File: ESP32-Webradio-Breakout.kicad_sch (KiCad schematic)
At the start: 46 parts, among them J1 AudioJack3, J2 Conn_01x02, P1 USB_C_Plug, Q1 BC817, Q2 BC817, Q3 BC817, SW1 RotaryEncoder_Switch, U1 AMS1117-3.3, U2 ESP32-WROOM-32, U3 CH340C, U4 PCF8574TS, U5 DS18B20

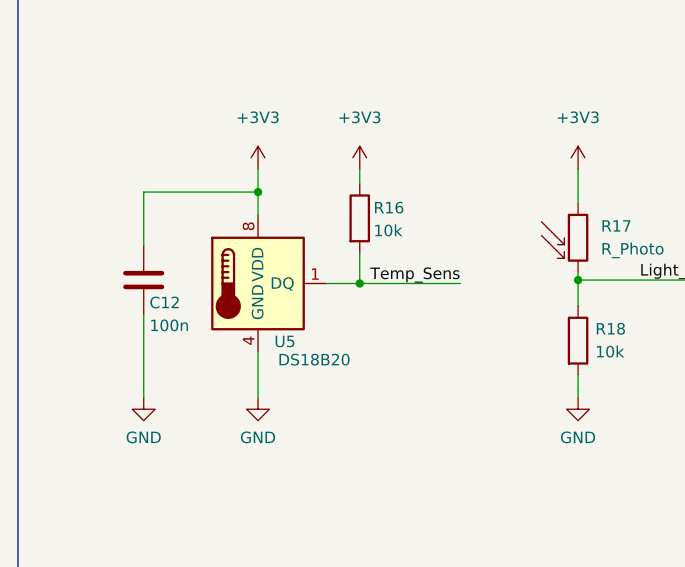
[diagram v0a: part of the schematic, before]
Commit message: Parts placement top side
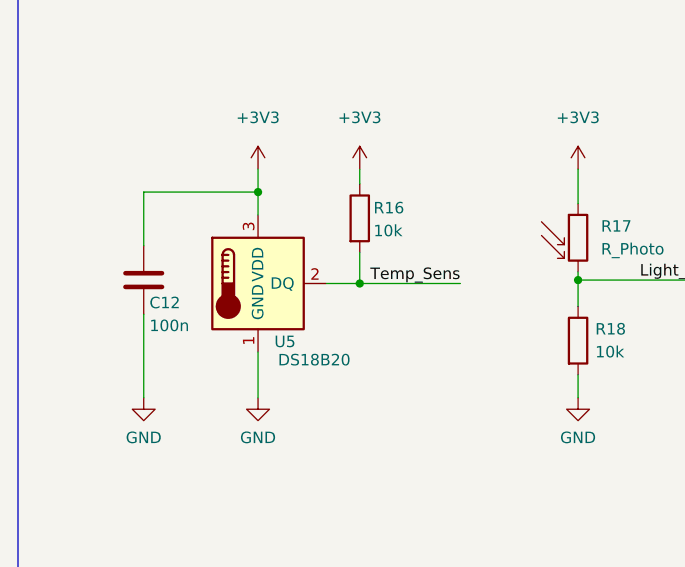
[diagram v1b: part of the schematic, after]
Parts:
- U5: footprint Package_SO:MSOP-8_3x3mm_P0.65mm -> Connector_PinHeader_2.54mm:PinHeader_1x03_P2.54mm_Vertical; symbol Sensor_Temperature:DS18B20U -> Sensor_Temperature:DS18B20
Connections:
- net +3V3: now also U5.3 (VDD); no longer U5.8 (VDD)
- net GND: now also U5.1 (GND); no longer U5.4 (GND)
- net Temp_Sens: now also U5.2 (DQ); no longer U5.1 (DQ)
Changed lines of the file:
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@@
     (pin "1")
   )
-  (symbol (lib_id "Sensor_Temperature:DS18B20U") (at 64.77 200.66 0) (unit 1)
+  (symbol (lib_id "Sensor_Temperature:DS18B20") (at 64.77 200.66 0) (unit 1)
     (in_bom yes) (on_board yes)
     (property "Reference" "U5" (id 0) (at 68.961 207.137 0)
@@
       (effects (font (size 1.27 1.27)) (justify right))
     )
-    (property "Footprint" "Package_SO:MSOP-8_3x3mm_P0.65mm" (id 2) (at 40.64 207.01 0)
+    (property "Footprint" "Connector_PinHeader_2.54mm:PinHeader_1x03_P2.54mm_Vertical" (id 2) (at 39.37 207.01 0)
       (effects (font (size 1.27 1.27)) hide)
     )
@@
     (pin "2")
     (pin "3")
-    (pin "4")
-    (pin "5")
-    (pin "6")
-    (pin "7")
-    (pin "8")
   )
   (symbol (lib_id "power:VCC") (at 240.03 166.37 0) (unit 1)
@@
     )
     (path "/a6b82443-9372-497e-a356-3173065d1b81"
-      (reference "U5") (unit 1) (value "DS18B20") (footprint "Package_SO:MSOP-8_3x3mm_P0.65mm")
-    )
-  )
+      (reference "U5") (unit 1) (value "DS18B20") (footprint "Connector_PinHeader_2.54mm:PinHeader_1x03_P2.54mm_Vertical")
+    )
+  )

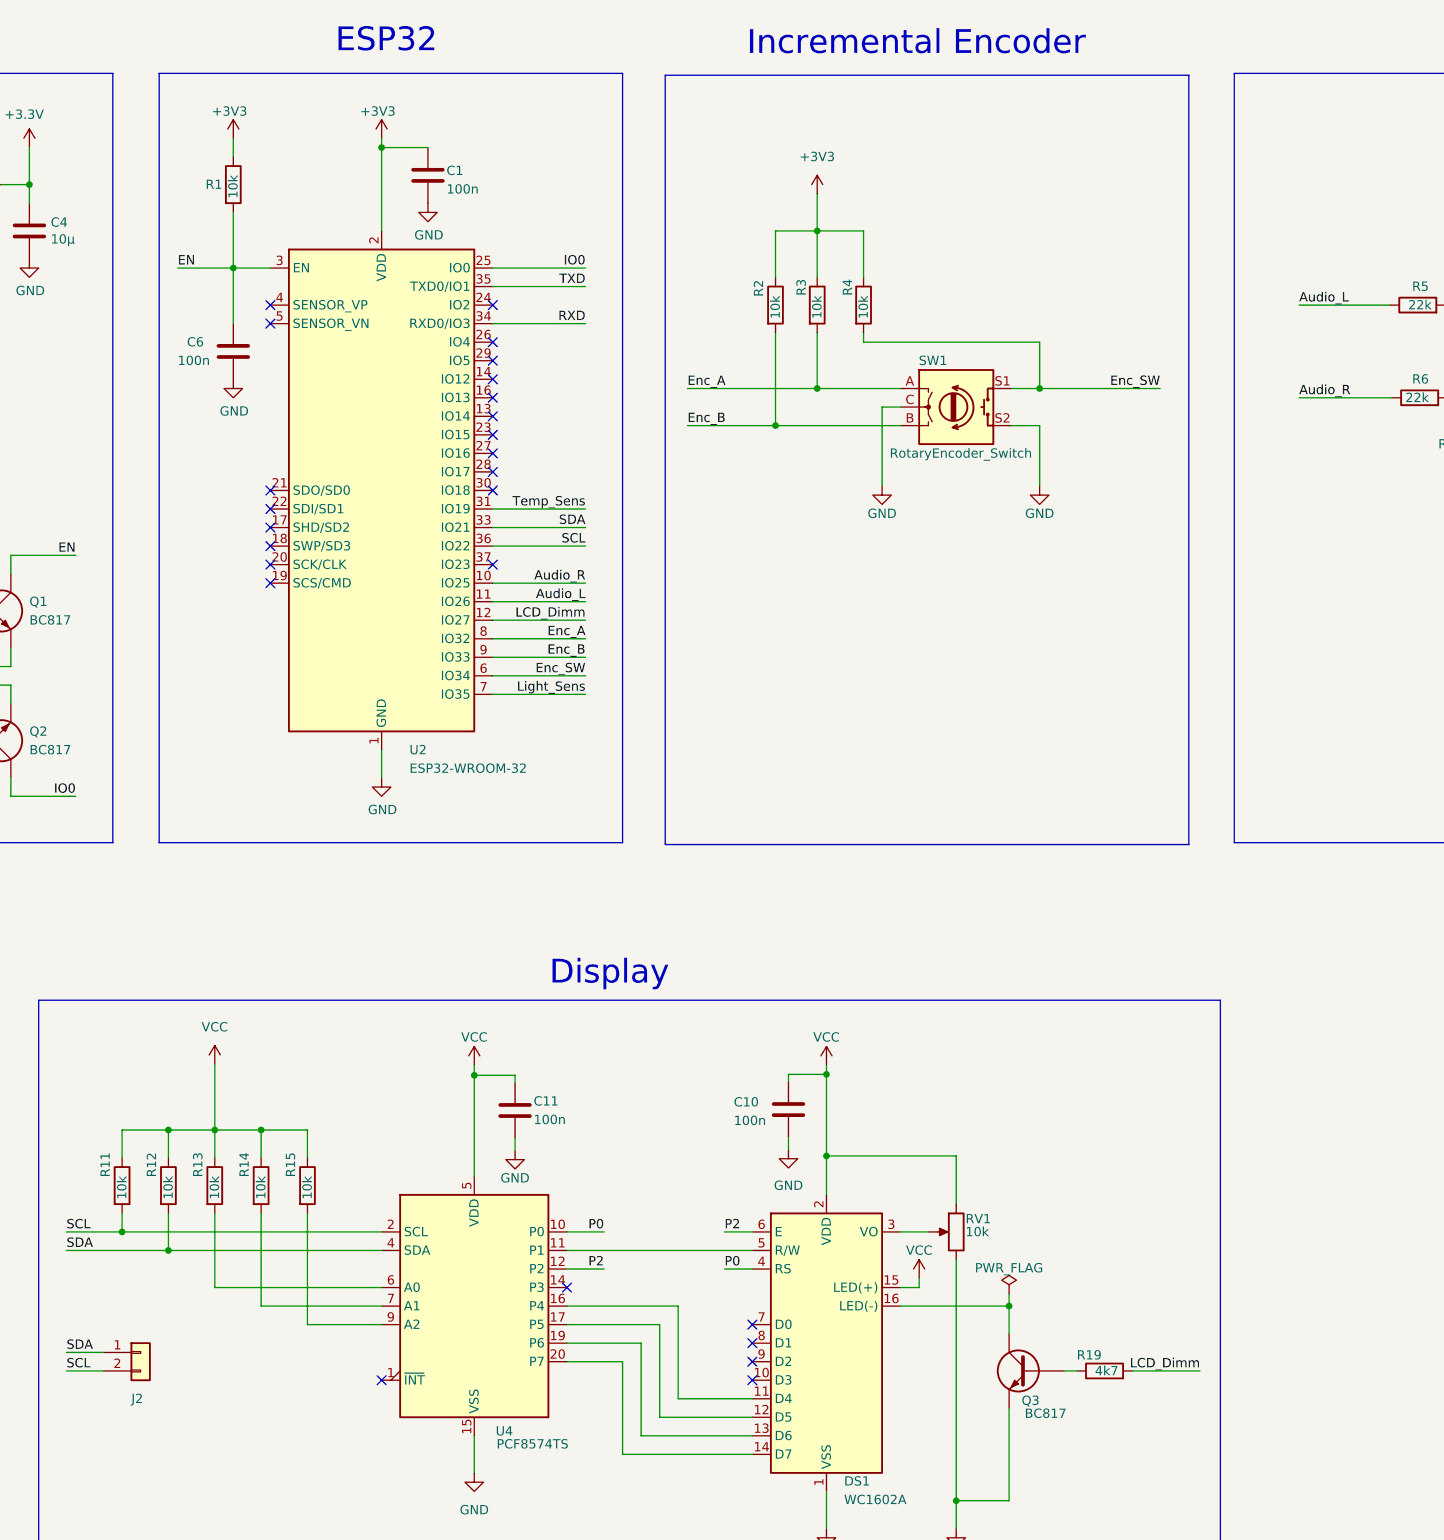
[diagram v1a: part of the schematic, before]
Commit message: Added pin for touch sensor Marked mounting holes as not in schematic
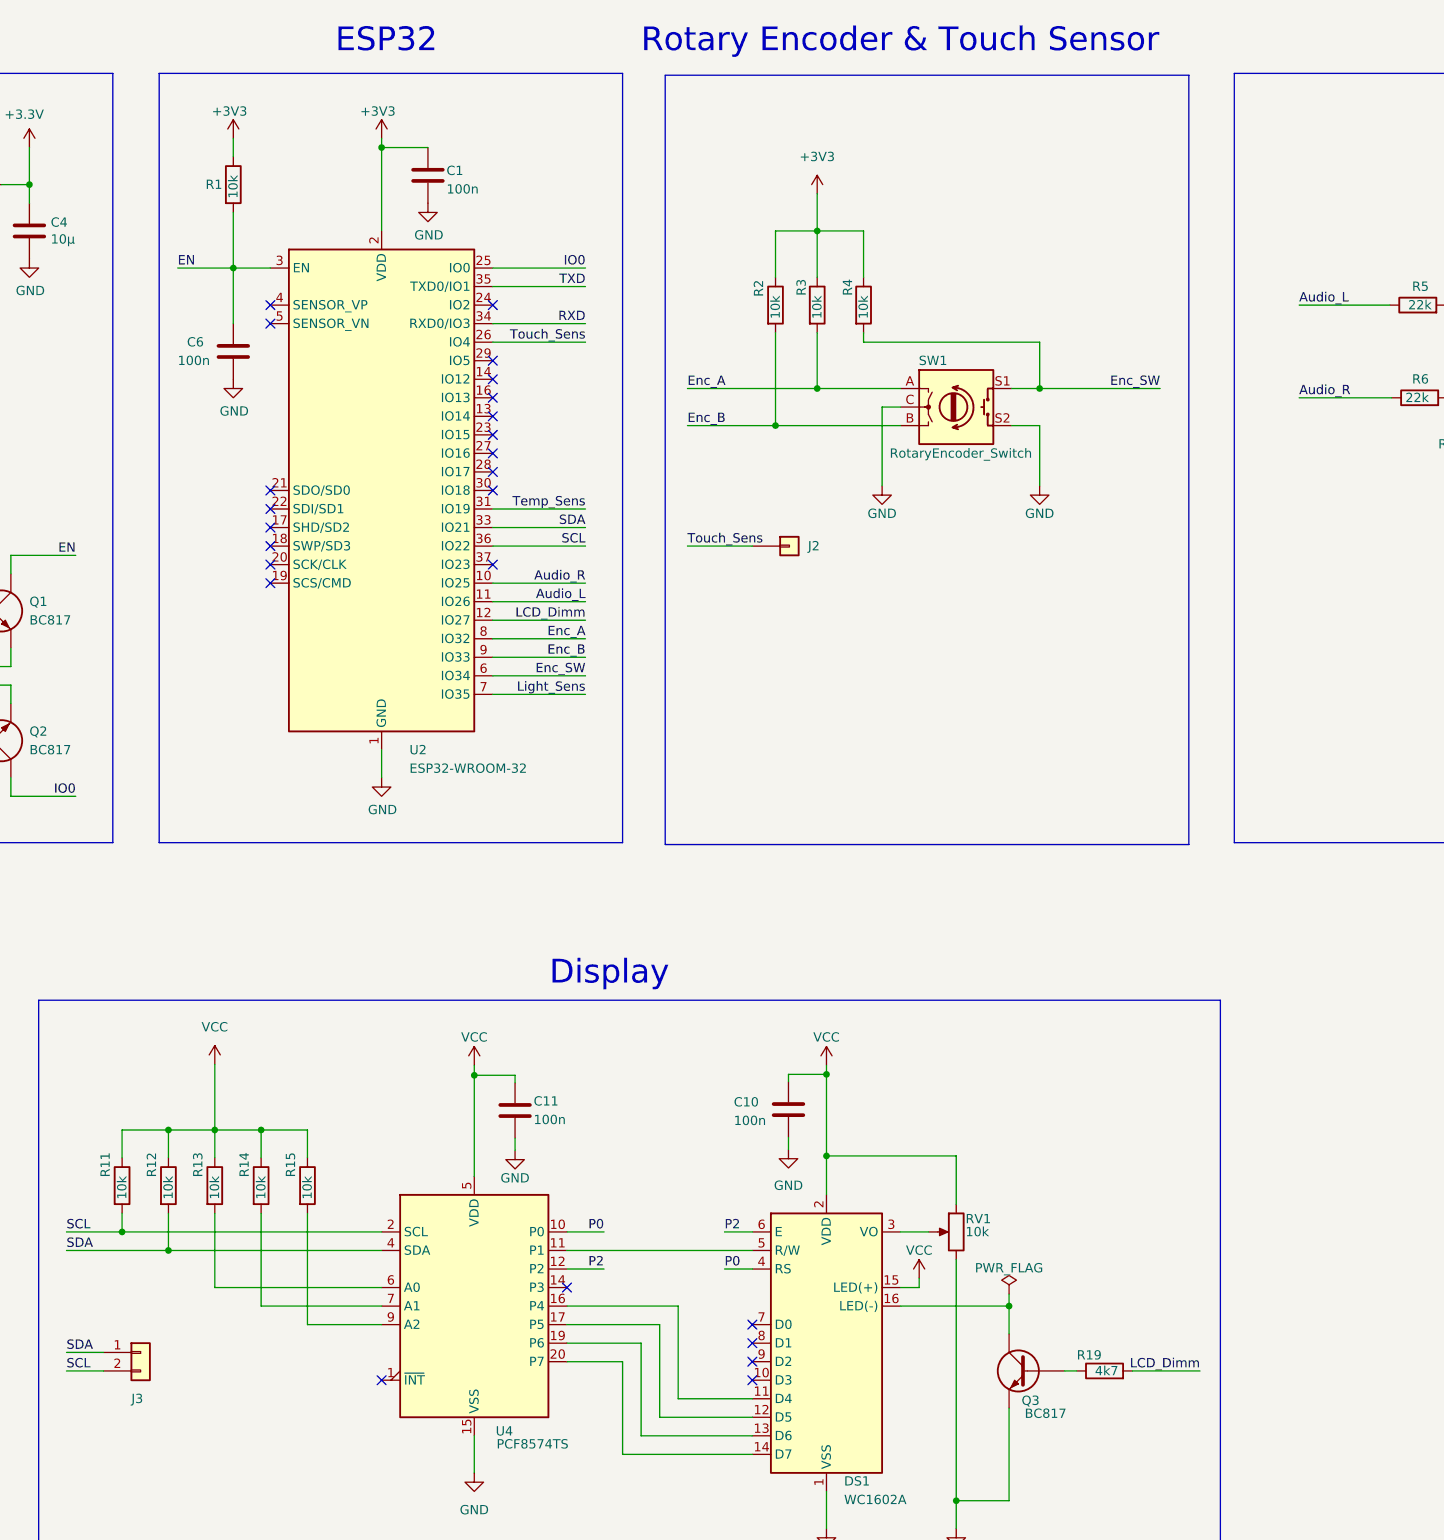
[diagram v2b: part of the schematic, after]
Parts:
- added J2: Conn_01x01, Connector_PinHeader_2.54mm:PinHeader_1x01_P2.54mm_Vertical, symbol Connector_Generic:Conn_01x01
- renumbered J2 to J3
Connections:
- net Touch_Sens: now reaches U2.26 (IO4)
- net Touch_Sens: now also J2.1 (Pin_1)
- no-connect marks 42 -> 41
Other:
- note added: "Rotary Encoder & Touch Sensor"
- note removed: "Incremental Encoder"
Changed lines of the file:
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@@
   (no_connect (at 194.31 77.47))
   (no_connect (at 194.31 74.93))
-  (no_connect (at 194.31 67.31))
   (no_connect (at 163.83 90.17))
   (no_connect (at 194.31 80.01))
@@
     (stroke (width 0) (type default) (color 0 0 0 0))
   )
+  (wire (pts (xy 194.31 67.31) (xy 207.01 67.31))
+    (stroke (width 0) (type default) (color 0 0 0 0))
+  )
   (wire (pts (xy 204.47 201.93) (xy 217.17 201.93))
     (stroke (width 0) (type default) (color 0 0 0 0))
@@
   )
   (wire (pts (xy 88.9 85.09) (xy 102.87 85.09))
+    (stroke (width 0) (type default) (color 0 0 0 0))
+  )
+  (wire (pts (xy 220.98 95.25) (xy 229.87 95.25))
     (stroke (width 0) (type default) (color 0 0 0 0))
   )
@@
     (effects (font (size 3.2512 3.2512)) (justify left bottom))
   )
-  (text "Incremental Encoder" (at 229.108 28.321 0)
+  (text "Rotary Encoder & Touch Sensor" (at 214.63 27.94 0)
     (effects (font (size 3.2512 3.2512)) (justify left bottom))
   )
@@
     (effects (font (size 1.27 1.27)) (justify right bottom))
   )
+  (label "Touch_Sens" (at 207.01 67.31 180)
+    (effects (font (size 1.27 1.27)) (justify right bottom))
+  )
   (label "EN" (at 137.16 96.52 180)
     (effects (font (size 1.27 1.27)) (justify right bottom))
@@
   )
   (label "SDA" (at 135.89 191.77 0)
+    (effects (font (size 1.27 1.27)) (justify left bottom))
+  )
+  (label "Touch_Sens" (at 220.98 95.25 0)
     (effects (font (size 1.27 1.27)) (justify left bottom))
   )
@@
   (symbol (lib_id "Connector_Generic:Conn_01x02") (at 146.05 205.74 0) (unit 1)
     (in_bom yes) (on_board yes)
-    (property "Reference" "J2" (id 0) (at 144.78 212.09 0)
+    (property "Reference" "J3" (id 0) (at 144.78 212.09 0)
       (effects (font (size 1.27 1.27)) (justify left))
     )
@@
     (pin "1")
   )
+  (symbol (lib_id "Connector_Generic:Conn_01x01") (at 234.95 95.25 0) (unit 1)
+    (in_bom yes) (on_board yes)
+    (property "Reference" "J2" (id 0) (at 237.49 95.25 0)
+      (effects (font (size 1.27 1.27)) (justify left))
+    )
+    (property "Value" "Conn_01x01" (id 1) (at 237.49 96.5199 0)
+      (effects (font (size 1.27 1.27)) (justify left) hide)
+    )
+    (property "Footprint" "Connector_PinHeader_2.54mm:PinHeader_1x01_P2.54mm_Vertical" (id 2) (at 234.95 95.25 0)
+      (effects (font (size 1.27 1.27)) hide)
+    )
+    (property "Datasheet" "~" (id 3) (at 234.95 95.25 0)
+      (effects (font (size 1.27 1.27)) hide)
+    )
+    (pin "1")
+  )
   (symbol (lib_id "power:VCC") (at 252.73 195.58 0) (unit 1)
     (in_bom yes) (on_board yes)
@@
       (reference "J1") (unit 1) (value "AudioJack3") (footprint "Connector_Audio:Jack_3.5mm_CUI_SJ-3523-SMT_Horizontal")
     )
+    (path "/855ad9f0-80ef-49c2-b466-44e7953643cd"
+      (reference "J2") (unit 1) (value "Conn_01x01") (footprint "Connector_PinHeader_2.54mm:PinHeader_1x01_P2.54mm_Vertical")
+    )
     (path "/387cf96c-c22c-4e93-837e-6545ff47a718"
-      (reference "J2") (unit 1) (value "Conn_01x02") (footprint "Connector_PinHeader_2.54mm:PinHeader_1x02_P2.54mm_Vertical")
+      (reference "J3") (unit 1) (value "Conn_01x02") (footprint "Connector_PinHeader_2.54mm:PinHeader_1x02_P2.54mm_Vertical")
     )
     (path "/a2f35872-afef-4c52-96b7-e07ab3768684"
